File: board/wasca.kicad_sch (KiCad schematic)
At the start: 67 parts

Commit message: Schematics & routing in progress
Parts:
- removed D1, D5: (no value), symbol wasca-rescue:LED_BCGR-Device
- added D1, D5: (no value), symbol Device:LED_BKGR
- C1, C2, C21, C22, C23, C25, C26, C38, C39, C42, C43, C44, C45, C46, C47, C48, C49, C50, C51, C52, C53, C55: value (none) -> 0.1uF; footprint (none) -> Capacitor_SMD:C_0603_1608Metric_Pad1.05x0.95mm_HandSolder
- C17, C3, C54: value (none) -> 4.7uF; footprint (none) -> Capacitor_SMD:C_0603_1608Metric_Pad1.05x0.95mm_HandSolder
- C24: value (none) -> 10uF; footprint (none) -> Capacitors_SMD:C_1206_HandSoldering
- CHAMFER_WARN1, CHAMFER_WARN2: value (none) -> CHAMFER_WARNING; footprint (none) -> wasca:CHAMFER_WARNING
- CN1: value (none) -> CARTRIDGE_EDGE_CONNECTOR; footprint (none) -> wasca:CARTRIDGE_EDGE_CONNECTOR2
- CN2: value (none) -> TFP09-2-12B; footprint (none) -> wasca:TFP09212B
- CN3: value (none) -> Conn_02x02_Odd_Even; footprint (none) -> Connector_PinHeader_2.54mm:PinHeader_2x02_P2.54mm_Vertical
- CN4: value (none) -> SODIMM-200; footprint (none) -> wasca:Conn_TE-DDR2-SODIMM-0.6-200P-doublesided
- CN6: value (none) -> USB_C_Receptacle_USB2.0; footprint (none) -> wasca:DX07S016JA1R1500
- D2, D3: value (none) -> LED_RGB; footprint (none) -> LED_SMD:LED_RGB_5050-6
- D4: value (none) -> BAT54C; footprint (none) -> Package_TO_SOT_SMD:SOT-23
- KICAD1: value (none) -> KICAD_LOGO; footprint (none) -> wasca:DESIGNED_WITH_KICAD_10X05
- R1, R10, R11, R19, R2, R24, R3: value (none) -> 470; footprint (none) -> Capacitor_SMD:C_0603_1608Metric_Pad1.08x0.95mm_HandSolder
- R13: value (none) -> 4K7; footprint (none) -> Capacitor_SMD:C_0603_1608Metric_Pad1.05x0.95mm_HandSolder
- R14: value (none) -> 10K; footprint (none) -> Capacitor_SMD:C_0603_1608Metric_Pad1.05x0.95mm_HandSolder
- R15, R16, R17, R8, R9: value (none) -> 33K; footprint (none) -> Capacitor_SMD:C_0603_1608Metric_Pad1.05x0.95mm_HandSolder
- R20: value (none) -> 5K1; footprint (none) -> Capacitor_SMD:C_0603_1608Metric_Pad1.08x0.95mm_HandSolder
- R21: value (none) -> 0; footprint (none) -> Capacitor_SMD:C_0603_1608Metric_Pad1.08x0.95mm_HandSolder
- SEGATA1: value (none) -> LOGO; footprint (none) -> wasca:Segata_Sanshiro
- U1, U2, U5: value (none) -> 74ALVC164245; footprint (none) -> Package_SO:TSSOP-48_6.1x12.5mm_P0.5mm
- U10, U11, U12, U8, U9: value (none) -> SN74LVC1T45DBV; footprint (none) -> Package_TO_SOT_SMD:SOT-23-6
- U13: value (none) -> ESP32_CAM_HALF; footprint (none) -> wasca:MODULE_ESP32-CAM-HALF
- U4: value (none) -> LD1117S33TR_SOT223; footprint (none) -> Package_TO_SOT_SMD:SOT-223-3_TabPin2
- VACHE1: value (none) -> LOGO; footprint (none) -> wasca:LOGO_VACHE_SIM
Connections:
- net GND: now also D1.2 (K), D5.2 (K)
- net at D2.5 (GA), R11.2: now also D1.3 (GA)
- net at D2.6 (RA), R10.2: now also D1.4 (RA)
- net at D2.4 (BA), R19.2: now also D1.1 (BA)
- net at D3.6 (RA), R1.2: now also D5.4 (RA)
- net at D3.5 (GA), R2.2: now also D5.3 (GA)
- net at D3.4 (BA), R3.2: now also D5.1 (BA)

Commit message: Post-migration cleanup, routing
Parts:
- removed CN1: CARTRIDGE_EDGE_CONNECTOR, wasca:CARTRIDGE_EDGE_CONNECTOR2, symbol 10M08SCE144I7G:CARTRIDGE_EDGE_CONNECTOR
- removed R24: 470, Capacitor_SMD:C_0603_1608Metric_Pad1.08x0.95mm_HandSolder, symbol Device:R
- added CN1: (no value), symbol wasca:CARTRIDGE_EDGE_CONNECTOR
- added R4, R5: (no value), symbol Device:R
- C1, C2, C21, C22, C23, C25, C26, C38, C39, C42, C43, C44, C45, C46, C47, C48, C49, C50, C51, C52, C53, C55: value 0.1uF -> (none); footprint Capacitor_SMD:C_0603_1608Metric_Pad1.05x0.95mm_HandSolder -> (none)
- C17, C3, C54: value 4.7uF -> (none); footprint Capacitor_SMD:C_0603_1608Metric_Pad1.05x0.95mm_HandSolder -> (none)
- C24: value 10uF -> (none); footprint Capacitors_SMD:C_1206_HandSoldering -> (none)
- CHAMFER_WARN1, CHAMFER_WARN2: value CHAMFER_WARNING -> (none); footprint wasca:CHAMFER_WARNING -> (none)
- CN2: value TFP09-2-12B -> (none); footprint wasca:TFP09212B -> (none)
- CN3: value Conn_02x02_Odd_Even -> (none); footprint Connector_PinHeader_2.54mm:PinHeader_2x02_P2.54mm_Vertical -> (none)
- CN4: value SODIMM-200 -> (none); footprint wasca:Conn_TE-DDR2-SODIMM-0.6-200P-doublesided -> (none)
- CN6: value USB_C_Receptacle_USB2.0 -> (none); footprint wasca:DX07S016JA1R1500 -> (none)
- D2, D3: value LED_RGB -> (none); footprint LED_SMD:LED_RGB_5050-6 -> (none)
- D4: value BAT54C -> (none); footprint Package_TO_SOT_SMD:SOT-23 -> (none)
- KICAD1: value KICAD_LOGO -> (none); footprint wasca:DESIGNED_WITH_KICAD_10X05 -> (none)
- R1, R10, R11, R19, R2, R3: value 470 -> (none); footprint Capacitor_SMD:C_0603_1608Metric_Pad1.08x0.95mm_HandSolder -> (none)
- R13: value 4K7 -> (none); footprint Capacitor_SMD:C_0603_1608Metric_Pad1.05x0.95mm_HandSolder -> (none)
- R14: value 10K -> (none); footprint Capacitor_SMD:C_0603_1608Metric_Pad1.05x0.95mm_HandSolder -> (none)
- R15, R16, R17, R8, R9: value 33K -> (none); footprint Capacitor_SMD:C_0603_1608Metric_Pad1.05x0.95mm_HandSolder -> (none)
- R20: value 5K1 -> (none); footprint Capacitor_SMD:C_0603_1608Metric_Pad1.08x0.95mm_HandSolder -> (none)
- R21: value 0 -> (none); footprint Capacitor_SMD:C_0603_1608Metric_Pad1.08x0.95mm_HandSolder -> (none)
- SEGATA1: value LOGO -> (none); footprint wasca:Segata_Sanshiro -> (none)
- U1, U2, U5: value 74ALVC164245 -> (none); footprint Package_SO:TSSOP-48_6.1x12.5mm_P0.5mm -> (none); symbol 10M08SCE144I7G:74ALVC164245 -> wasca:74ALVC164245
- U10, U11, U12, U8, U9: value SN74LVC1T45DBV -> (none); footprint Package_TO_SOT_SMD:SOT-23-6 -> (none)
- U13: value ESP32_CAM_HALF -> (none); footprint wasca:MODULE_ESP32-CAM-HALF -> (none)
- U4: value LD1117S33TR_SOT223 -> (none); footprint Package_TO_SOT_SMD:SOT-223-3_TabPin2 -> (none)
- VACHE1: value LOGO -> (none); footprint wasca:LOGO_VACHE_SIM -> (none)
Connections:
- net +5V_SATURN: now also CN1.A1 (VCC), CN1.A2 (VCC), CN1.A27 (VCC), CN1.A67 (VCC), CN1.B1 (VCC), CN1.B2 (VCC), CN1.B27 (VCC), CN1.B67 (VCC), R4.1
- net +5V_SYS: now also C38.1
- net +5V_USB: now also R13.1; no longer R13.2
- net 5V_SATURN_DETECT: now also R4.2, R5.1
- net ABUS_3V_IRQ: no longer CN4.145
- net ABUS_A1: now also CN1.A45 (AA1)
- net ABUS_A10: now also CN1.A44 (AA10)
- net ABUS_A11: now also CN1.A43 (AA11)
- net ABUS_A12: now also CN1.A38 (AA12)
- net ABUS_A13: now also CN1.A39 (AA13)
- net ABUS_A14: now also CN1.B37 (AA14)
- net ABUS_A15: now also CN1.A37 (AA15)
- net ABUS_A16: now also CN1.B35 (AA16)
- net ABUS_A17: now also CN1.A35 (AA17)
- net ABUS_A18: now also CN1.B34 (AA18)
- net ABUS_A19: now also CN1.A34 (AA19)
- net ABUS_A2: now also CN1.B44 (AA2)
- net ABUS_A20: now also CN1.B33 (AA20)
- net ABUS_A21: now also CN1.A33 (AA21)
- net ABUS_A22: now also CN1.B32 (AA22)
- net ABUS_A23: now also CN1.A32 (AA23)
- net ABUS_A24: now also CN1.B31 (AA24)
- net ABUS_A3: now also CN1.B43 (AA3)
- net ABUS_A4: now also CN1.B42 (AA4)
- net ABUS_A5: now also CN1.B40 (AA5)
- net ABUS_A6: now also CN1.B39 (AA6)
- net ABUS_A7: now also CN1.B38 (AA7)
- net ABUS_A8: now also CN1.A40 (AA8)
- net ABUS_A9: now also CN1.A42 (AA9)
- net ABUS_CS0: now also CN1.A47 (ACS0)
- net ABUS_CS1: now also CN1.B48 (ACS1)
- net ABUS_CS2: now also CN1.A48 (ACS2)
- net ABUS_D0: now also CN1.A55 (AD0)
- net ABUS_D1: now also CN1.A56 (AD1)
- net ABUS_D10: now also CN1.A62 (AD10)
- net ABUS_D11: now also CN1.A63 (AD11)
- net ABUS_D12: now also CN1.B63 (AD12)
- net ABUS_D13: now also CN1.B62 (AD13)
- net ABUS_D14: now also CN1.B61 (AD14)
- net ABUS_D15: now also CN1.B60 (AD15)
- net ABUS_D2: now also CN1.A57 (AD2)
- net ABUS_D3: now also CN1.A58 (AD3)
- net ABUS_D4: now also CN1.B58 (AD4)
- net ABUS_D5: now also CN1.B57 (AD5)
- net ABUS_D6: now also CN1.B56 (AD6)
- net ABUS_D7: now also CN1.B55 (AD7)
- net ABUS_D8: now also CN1.A60 (AD8)
- net ABUS_D9: now also CN1.A61 (AD9)
- net ABUS_IRQ: now also CN1.B53 (AIRQ)
- net ABUS_RD: now also CN1.B47 (ARD)
- net ABUS_WR0: now also CN1.A49 (AWR0)
- net ABUS_WR1: now also CN1.B49 (AWR1)
- net ESP32_CS: now also CN4.152; no longer CN4.156
- net ESP32_MISO: now also CN4.156; no longer CN4.150
- net ESP32_MOSI: now also CN4.154; no longer CN4.152
- net ESP32_SCK: now also CN4.150; no longer CN4.154
- net GND: now also R14.2, CN1.A13 (GND), CN1.A18 (GND), CN1.A23 (GND), CN1.A29 (GND), CN1.A36 (GND), CN1.A41 (GND), CN1.A46 (GND), CN1.A54 (GND), CN1.A59 (GND), CN1.A64 (GND), CN1.A65 (GND), CN1.A8 (GND), CN1.B13 (GND), CN1.B18 (GND), CN1.B23 (GND), CN1.B29 (GND), CN1.B36 (GND), CN1.B41 (GND), CN1.B46 (GND), CN1.B54 (GND), CN1.B59 (GND), CN1.B64 (GND), CN1.B65 (GND), CN1.B7 (GND), CN1.B8 (GND), R5.2; no longer R14.1
- net IBCK: now also CN1.A5 (IBCK)
- net IBCK_3V: now also CN4.153; no longer CN4.151
- net ILRCK: now also CN1.A6 (ILRCK)
- net ILRCK_3V: now also CN4.151; no longer CN4.155
- net ISD: now also CN1.A4 (ISD)
- net ISD_3V: now also CN4.155; no longer CN4.153
- net LEDB: now also CN4.132; no longer CN4.126
- net LEDG: now also CN4.130; no longer CN4.124
- net LEDR: now also CN4.128; no longer CN4.122
- net RESET: now also CN1.A3 (SYSRES)
- net SCSPCLK: now also CN1.A7 (SCSPCLK)
- net SD_CLK: now also CN4.116; no longer CN4.120
- net SD_CMD: now also CN4.122; no longer CN4.110
- net SD_DAT0: now also CN4.114; no longer CN4.112
- net SD_DAT1: now also CN4.120; no longer CN4.116
- net SD_DAT2: now also CN4.124; no longer CN4.118
- net SD_DAT3: now also CN4.118; no longer CN4.114
- net SD_DET_A: now also CN4.110; no longer CN4.130
- net SD_DET_B: now also CN4.112; no longer CN4.132
- net SSEL: now also CN1.B3 (SSEL)
- net 5V_USB_DETECT: now reaches CN4.143
- net 5V_USB_DETECT: now also R13.2, R14.1
- removed net VBUS_SENSE: R13.1, R14.2
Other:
- moved on the sheet: C38

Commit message: Further cleanup
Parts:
- C1, C2, C21, C22, C23, C25, C26, C38, C39, C42, C43, C44, C45, C46, C47, C48, C49, C50, C51, C52, C53, C55: value (none) -> 0.1uF; footprint (none) -> Capacitor_SMD:C_0603_1608Metric_Pad1.08x0.95mm_HandSolder
- C17, C3, C54: value (none) -> 4.7uF; footprint (none) -> Capacitor_SMD:C_0603_1608Metric_Pad1.08x0.95mm_HandSolder
- C24: value (none) -> 10uF; footprint (none) -> Capacitor_SMD:C_1206_3216Metric_Pad1.33x1.80mm_HandSolder
- CHAMFER_WARN1, CHAMFER_WARN2: value (none) -> CHAMFER_WARNING; footprint (none) -> wasca:CHAMFER_WARNING
- CN1: value (none) -> CARTRIDGE_EDGE_CONNECTOR; footprint (none) -> wasca:CARTRIDGE_EDGE_CONNECTOR2
- CN2: value (none) -> TFP09-2-12B; footprint (none) -> TFP09212B
- CN3: value (none) -> Conn_02x02_Odd_Even; footprint (none) -> Connector_PinHeader_2.54mm:PinHeader_2x02_P2.54mm_Vertical
- CN4: value (none) -> SODIMM-200; footprint (none) -> wasca:Conn_TE-DDR2-SODIMM-0.6-200P-doublesided
- CN6: value (none) -> USB_C_Receptacle_USB2.0; footprint (none) -> wasca:DX07S016JA1R1500
- D1, D5: value (none) -> LED_BKGR; footprint (none) -> LED_THT:LED_D5.0mm-4_RGB
- D2, D3: value (none) -> LED_RGB; footprint (none) -> LED_SMD:LED_RGB_5050-6
- D4: value (none) -> BAT54C; footprint (none) -> Package_TO_SOT_SMD:SOT-23
- KICAD1: value (none) -> KICAD_LOGO; footprint (none) -> wasca:DESIGNED_WITH_KICAD_10X05
- R1, R10, R11, R19, R2, R3: value (none) -> 470; footprint (none) -> Resistor_SMD:R_0603_1608Metric_Pad0.98x0.95mm_HandSolder
- R13, R4: value (none) -> 4K7; footprint (none) -> Resistor_SMD:R_0603_1608Metric_Pad0.98x0.95mm_HandSolder
- R14, R5: value (none) -> 10K; footprint (none) -> Resistor_SMD:R_0603_1608Metric_Pad0.98x0.95mm_HandSolder
- R15, R16, R17, R8, R9: value (none) -> 33K; footprint (none) -> Resistor_SMD:R_0603_1608Metric_Pad0.98x0.95mm_HandSolder
- R20: value (none) -> 5K1; footprint (none) -> Capacitor_SMD:C_0603_1608Metric_Pad1.08x0.95mm_HandSolder
- R21: value (none) -> 0; footprint (none) -> Resistor_SMD:R_0603_1608Metric_Pad0.98x0.95mm_HandSolder
- SEGATA1: value (none) -> LOGO; footprint (none) -> wasca:Segata_Sanshiro
- U1, U2, U5: value (none) -> 74ALVC164245; footprint (none) -> Package_SO:TSSOP-48_6.1x12.5mm_P0.5mm
- U10, U11, U12, U8, U9: value (none) -> SN74LVC1T45DBV; footprint (none) -> Package_TO_SOT_SMD:SOT-23-6
- U13: value (none) -> ESP32_CAM_HALF; footprint (none) -> wasca:MODULE_ESP32-CAM-HALF
- U4: value (none) -> LD1117S33TR_SOT223; footprint (none) -> Package_TO_SOT_SMD:SOT-223-3_TabPin2
- VACHE1: value (none) -> LOGO; footprint (none) -> wasca:LOGO_VACHE_SIM

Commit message: USB removed. Second SDRAM added. Reroute (incomplete)
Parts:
- removed CN6: USB_C_Receptacle_USB2.0, wasca:DX07S016JA1R1500, symbol Connector:USB_C_Receptacle_USB2.0
- removed D3: LED_RGB, LED_SMD:LED_RGB_5050-6, symbol Device:LED_RGB
- removed D5: LED_BKGR, LED_THT:LED_D5.0mm-4_RGB, symbol Device:LED_BKGR
- removed R1, R2, R3: 470, Resistor_SMD:R_0603_1608Metric_Pad0.98x0.95mm_HandSolder, symbol Device:R
- removed R13: 4K7, Resistor_SMD:R_0603_1608Metric_Pad0.98x0.95mm_HandSolder, symbol Device:R
- removed R14: 10K, Resistor_SMD:R_0603_1608Metric_Pad0.98x0.95mm_HandSolder, symbol Device:R
- removed R20: 5K1, Capacitor_SMD:C_0603_1608Metric_Pad1.08x0.95mm_HandSolder, symbol Device:R
- added C4: 0.1uF, Capacitor_SMD:C_0603_1608Metric_Pad1.08x0.95mm_HandSolder, symbol Device:C_Small
- added U3: MT48LC16M16A2TG, Package_SO:TSOP-II-54_22.2x10.16mm_P0.8mm, symbol Memory_RAM:MT48LC16M16A2TG
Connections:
- net +3_3V: now also C4.1, U3.1 (VDD), U3.14 (VDD), U3.27 (VDD), U3.3 (VDDQ), U3.43 (VDDQ), U3.49 (VDDQ), U3.9 (VDDQ)
- net +5V_SYS: now also C52.1, C53.1, C54.1
- net 5V_SATURN_DETECT: now also CN4.54; no longer CN4.98
- net ABUS_3V_A1: now also CN4.51; no longer CN4.61
- net ABUS_3V_A10: now also CN4.49; no longer CN4.59
- net ABUS_3V_A11: now also CN4.41; no longer CN4.57
- net ABUS_3V_A12: now also CN4.69; no longer CN4.75
- net ABUS_3V_A13: now also CN4.67; no longer CN4.73
- net ABUS_3V_A14: now also CN4.119; no longer CN4.121
- net ABUS_3V_A15: now also CN4.71; no longer CN4.77
- net ABUS_3V_A16: now also CN4.121; no longer CN4.123
- net ABUS_3V_A17: now also CN4.87; no longer CN4.89
- net ABUS_3V_A18: now also CN4.123; no longer CN4.125
- net ABUS_3V_A19: now also CN4.85; no longer CN4.87
- net ABUS_3V_A2: now also CN4.103; no longer CN4.109
- net ABUS_3V_A20: now also CN4.125; no longer CN4.127
- net ABUS_3V_A21: now also CN4.83; no longer CN4.85
- net ABUS_3V_A22: now also CN4.127; no longer CN4.129
- net ABUS_3V_A23: now also CN4.81; no longer CN4.83
- net ABUS_3V_A24: now also CN4.129; no longer CN4.131
- net ABUS_3V_A3: now also CN4.109; no longer CN4.111
- net ABUS_3V_A4: now also CN4.111; no longer CN4.113
- net ABUS_3V_A5: now also CN4.113; no longer CN4.115
- net ABUS_3V_A6: now also CN4.115; no longer CN4.117
- net ABUS_3V_A7: now also CN4.117; no longer CN4.119
- net ABUS_3V_A8: now also CN4.65; no longer CN4.71
- net ABUS_3V_A9: now also CN4.63; no longer CN4.69
- net ABUS_3V_CS0: now also CN4.57; no longer CN4.63
- net ABUS_3V_CS1: now also CN4.99; no longer CN4.101
- net ABUS_3V_CS2: now also CN4.59; no longer CN4.65
- net ABUS_3V_IRQ: now also CN4.93; no longer CN4.95
- net ABUS_3V_MUX_DATA_DIR: now also CN4.91; no longer CN4.93
- net ABUS_3V_RD: now also CN4.101; no longer CN4.103
- net ABUS_3V_WR0: now also CN4.61; no longer CN4.67
- net ABUS_3V_WR1: now also CN4.97; no longer CN4.99
- net BUFFERS_OE: now also CN4.77; no longer CN4.79
- net GND: now also CN4.89, C4.2, U3.12 (VSSQ), U3.23 (A0), U3.28 (VSS), U3.41 (VSS), U3.46 (VSSQ), U3.52 (VSSQ), U3.54 (VSS), U3.6 (VSSQ)
- net IBCK_3V: now also CN4.151; no longer CN4.153
- net ILRCK_3V: now also CN4.149; no longer CN4.151
- net IRQ_OUT_ENABLE: now also CN4.145, CN4.95; no longer CN4.147, CN4.97
- net ISD_3V: now also CN4.153; no longer CN4.155
- net LEDB: now also CN4.94; no longer CN4.132
- net LEDG: now also CN4.92; no longer CN4.130
- net LEDR: now also CN4.90; no longer CN4.128
- net RESET_3V: now also CN4.79; no longer CN4.81
- net SCSPCLK: now also CN4.147; no longer CN4.149
- net SD_CLK: now also CN4.44; no longer CN4.116
- net SD_CMD: now also CN4.50; no longer CN4.122
- net SD_DAT0: now also CN4.42; no longer CN4.114
- net SD_DAT1: now also CN4.52; no longer CN4.120
- net SD_DAT2: now also CN4.48; no longer CN4.124
- net SD_DAT3: now also CN4.46; no longer CN4.118
- net SD_DET_A: now also CN4.73; no longer CN4.110
- net SD_DET_B: now also CN4.75; no longer CN4.112
- net SSEL_3V: now also CN4.148; no longer CN4.96
- net SDRAM_AUX_DQ2: now reaches CN4.100
- net SDRAM_AUX_DQ2: now also U3.5 (DQ2)
- net SDRAM_AUX_CS: now reaches CN4.126
- net SDRAM_AUX_CS: now also U3.19 (~{CS})
- net SDRAM_AUX_A2: now reaches CN4.133
- net SDRAM_AUX_A2: now also U3.25 (A2)
- net SDRAM_AUX_CLK: now reaches CN4.134
- net SDRAM_AUX_CLK: now also U3.38 (CLK)
- net SDRAM_AUX_A3: now reaches CN4.135
- net SDRAM_AUX_A3: now also U3.26 (A3)
- net SDRAM_AUX_A4: now reaches CN4.137
- net SDRAM_AUX_A4: now also U3.29 (A4)
- net SDRAM_AUX_A5: now reaches CN4.139
- net SDRAM_AUX_A5: now also U3.30 (A5)
- net SDRAM_AUX_A12: now reaches CN4.140
- net SDRAM_AUX_A12: now also U3.36 (A12)
- net SDRAM_AUX_A6: now reaches CN4.141
- net SDRAM_AUX_A6: now also U3.31 (A6)
- removed net +5V_USB: C52.1, C53.1, C54.1, D4.2
- net 5V_USB_DETECT renamed SDRAM_AUX_A7
- net SDRAM_AUX_A7: now also U3.32 (A7)
- net DBG_UART_RX renamed SDRAM_AUX_A11
- net SDRAM_AUX_A11: now also U3.35 (A11)
- net DBG_UART_TX renamed SDRAM_AUX_A10
- net SDRAM_AUX_A10: now also U3.22 (A10)
- net LED2B renamed SDRAM_AUX_A9
- net SDRAM_AUX_A9: now also U3.34 (A9)
- net LED2G renamed SDRAM_AUX_A8
- net SDRAM_AUX_A8: now also U3.33 (A8)
- net LED2R: no longer names the net of CN4.142
- net USB_DM renamed SDRAM_AUX_DQ3
- net SDRAM_AUX_DQ3: now also U3.7 (DQ3)
- net USB_DP renamed SDRAM_AUX_DQ4
- net SDRAM_AUX_DQ4: now also U3.8 (DQ4)
- new net SDRAM_AUX_A1: CN4.131, U3.24 (A1)
- new net SDRAM_AUX_BA0: CN4.128, U3.20 (BA0)
- new net SDRAM_AUX_BA1: CN4.130, U3.21 (BA1)
- new net SDRAM_AUX_CAS: CN4.120, U3.17 (~{CAS})
- new net SDRAM_AUX_CKE: CN4.132, U3.37 (CKE)
- new net SDRAM_AUX_DQ0: CN4.96, U3.2 (DQ0)
- new net SDRAM_AUX_DQ1: CN4.98, U3.4 (DQ1)
- new net SDRAM_AUX_DQ5: CN4.110, U3.10 (DQ5)
- new net SDRAM_AUX_DQ6: CN4.112, U3.11 (DQ6)
- new net SDRAM_AUX_DQ7: CN4.114, U3.13 (DQ7)
- new net SDRAM_AUX_DQM0: CN4.116, U3.15 (DQML)
- new net SDRAM_AUX_DQM1: CN4.124, U3.39 (DQMH)
- new net SDRAM_AUX_RAS: CN4.122, U3.18 (~{RAS})
- new net SDRAM_AUX_WE: CN4.118, U3.16 (~{WE})
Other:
- note removed: "Compatible connectors: JAE DX07S016JA1R1500 JAE DX07S016JA3R1500 HROPARTS TYPE-C-31-M-12 HROPARTS TYPE-C-31-M-14 XKB U262-161N-4BVC11 Jing Ext. C167321"
- moved on the sheet: C52, C53, C54, R4, R5

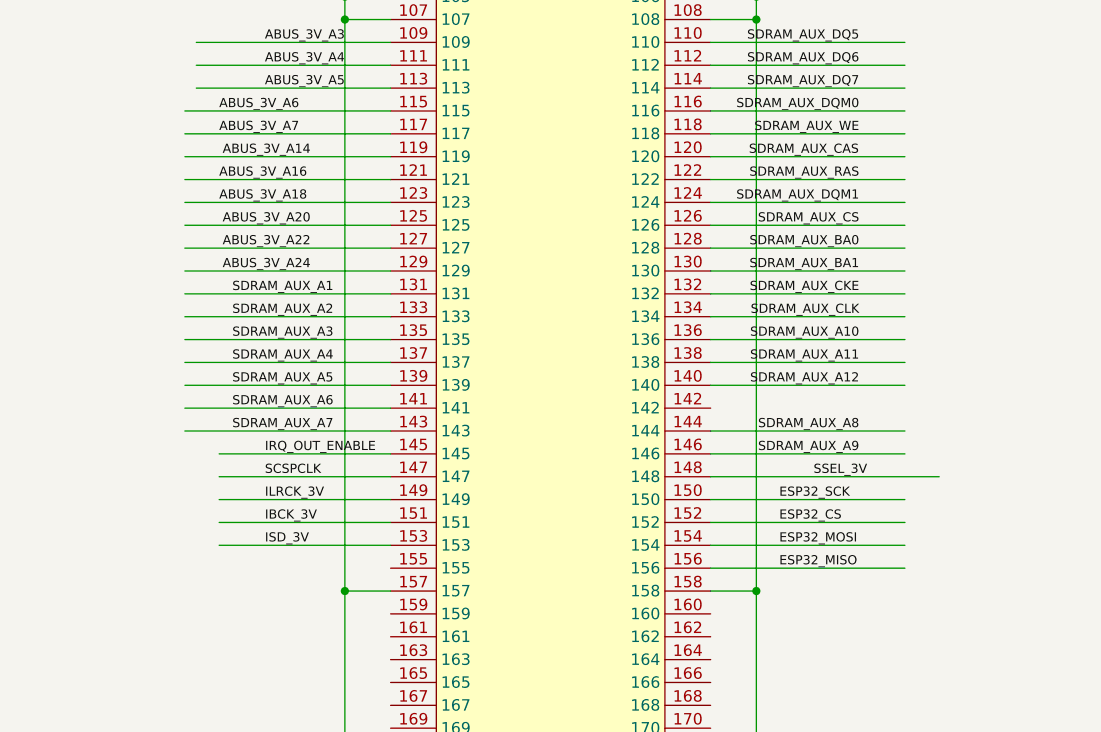
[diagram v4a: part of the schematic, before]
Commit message: Reroute complete, cleanup pending.
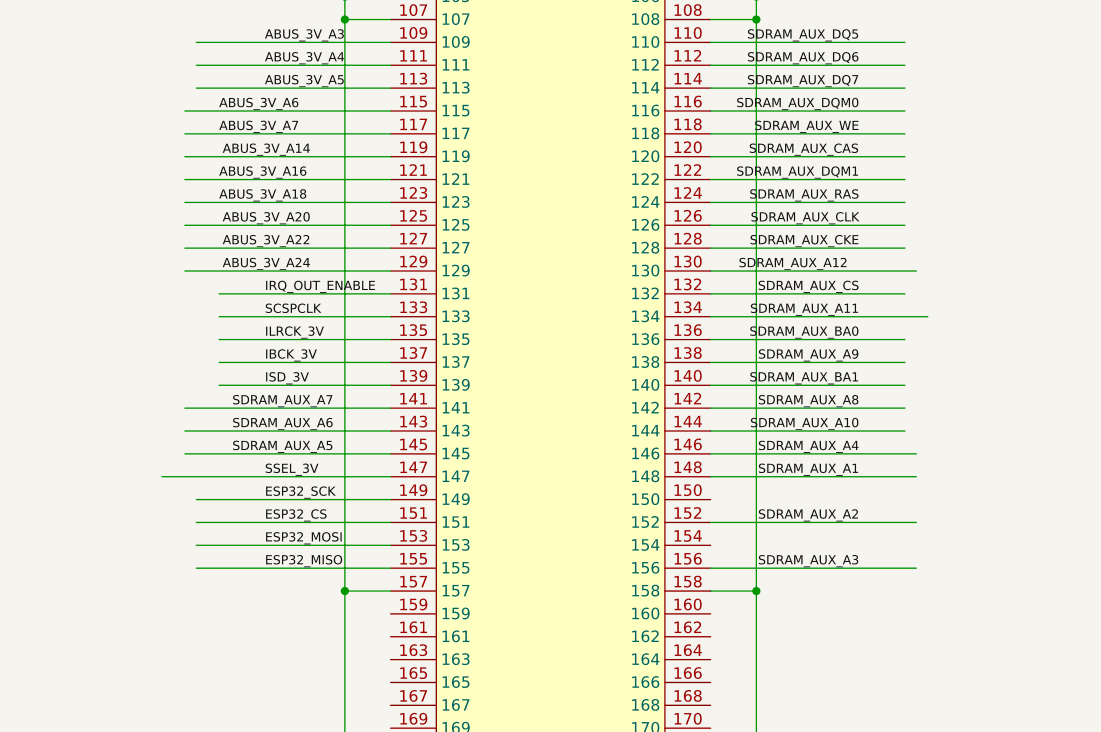
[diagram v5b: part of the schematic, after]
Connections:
- net ESP32_CS: now also CN4.151; no longer CN4.152
- net ESP32_MISO: now also CN4.155; no longer CN4.156
- net ESP32_MOSI: now also CN4.153; no longer CN4.154
- net ESP32_SCK: now also CN4.149; no longer CN4.150
- net IBCK_3V: now also CN4.137; no longer CN4.151
- net ILRCK_3V: now also CN4.135; no longer CN4.149
- net IRQ_OUT_ENABLE: now also CN4.131; no longer CN4.145
- net ISD_3V: now also CN4.139; no longer CN4.153
- net SCSPCLK: now also CN4.133; no longer CN4.147
- net SDRAM_AUX_A1: now also CN4.148; no longer CN4.131
- net SDRAM_AUX_A10: now also CN4.144; no longer CN4.136
- net SDRAM_AUX_A11: now also CN4.134; no longer CN4.138
- net SDRAM_AUX_A12: now also CN4.130; no longer CN4.140
- net SDRAM_AUX_A2: now also CN4.152; no longer CN4.133
- net SDRAM_AUX_A3: now also CN4.156; no longer CN4.135
- net SDRAM_AUX_A4: now also CN4.146; no longer CN4.137
- net SDRAM_AUX_A5: now also CN4.145; no longer CN4.139
- net SDRAM_AUX_A6: now also CN4.143; no longer CN4.141
- net SDRAM_AUX_A7: now also CN4.141; no longer CN4.143
- net SDRAM_AUX_A8: now also CN4.142; no longer CN4.144
- net SDRAM_AUX_A9: now also CN4.138; no longer CN4.146
- net SDRAM_AUX_BA0: now also CN4.136; no longer CN4.128
- net SDRAM_AUX_BA1: now also CN4.140; no longer CN4.130
- net SDRAM_AUX_CKE: now also CN4.128; no longer CN4.132
- net SDRAM_AUX_CLK: now also CN4.126; no longer CN4.134
- net SDRAM_AUX_CS: now also CN4.132; no longer CN4.126
- net SDRAM_AUX_DQM1: now also CN4.122; no longer CN4.124
- net SDRAM_AUX_RAS: now also CN4.124; no longer CN4.122
- net SSEL_3V: now also CN4.147; no longer CN4.148
